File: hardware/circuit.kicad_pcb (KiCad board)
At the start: 4 copper layers, 59.5 x 53.2 mm, 71 parts, among them J1 VBUS input fly-leads, J2 Orange TinySLED, J3 Orange TinySLED, J4 AM32 dual ESC, Q1 AO3402, U1 Seeed XIAO RP2350, U10 SK9822-EC20, U11 SN74HC595PWR, U12 SK9822-EC20, U2 AP63205WU-7, U4 LSM6DSV320XTR, U5 H3LIS331DLTR, U6 H3LIS331DLTR, U7 BetaFPV ELRS Lite, U8 SN74AHCT1G125, U9 SN74AHCT1G125

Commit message: chore: swap holes to the other side
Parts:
- moved Mountinghole-2 50.5 mm to (128.5, 121.0)
- moved MountingHole-2 48.4 mm to (79.0, 78.2)
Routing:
- net /LED_OE_N: track 74.2 -> 70.2 mm, vias 1 -> 2
- net GND: track 148.3 -> 147.3 mm, vias 53 -> 45
- net 5V: vias 8 -> 18
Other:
- board size 59.5 x 53.2 mm -> 59.5 x 53.5 mm

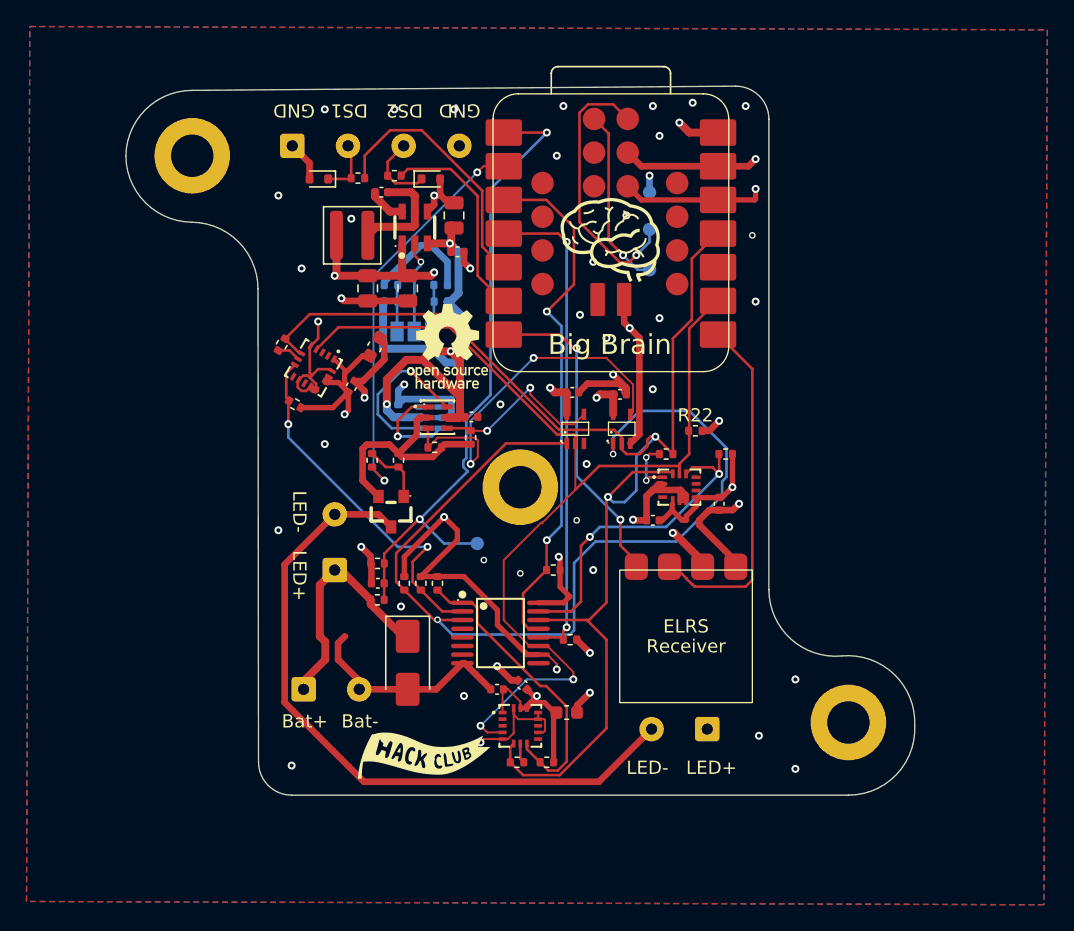
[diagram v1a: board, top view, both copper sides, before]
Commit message: feat: extend pcb to fit better in cad
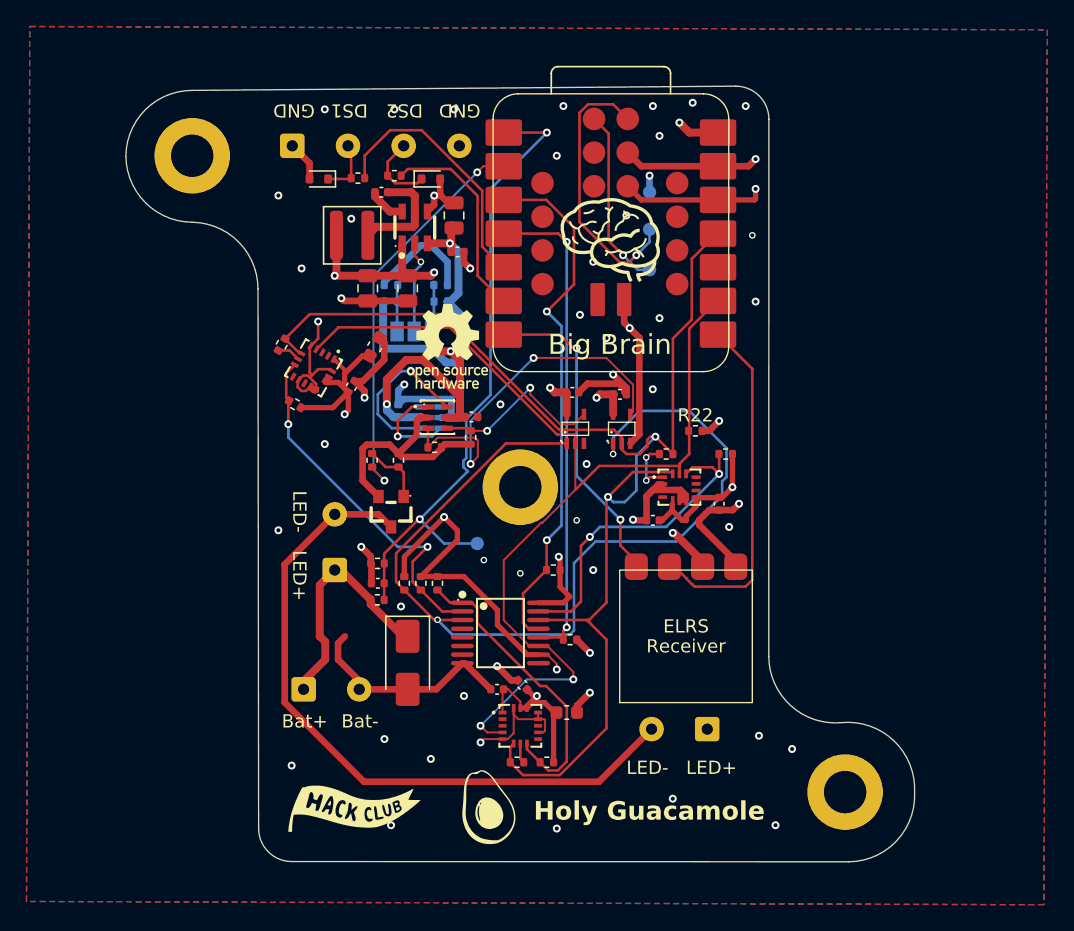
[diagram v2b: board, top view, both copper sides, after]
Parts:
- added gauc: LOGO, LOGO, F.Cu at (101.2, 127.5)
- moved G*** 6.60 mm to (91.2, 127.5)
- moved Mountinghole-2 5.26 mm to (128.2, 126.2)
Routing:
- net GND: vias 45 -> 56
- net 5V: vias 18 -> 10
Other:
- board size 59.5 x 53.5 mm -> 59.5 x 58.5 mm
- board text added: "Holy Guacamole"
